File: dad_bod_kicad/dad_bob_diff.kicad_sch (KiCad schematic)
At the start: 66 parts

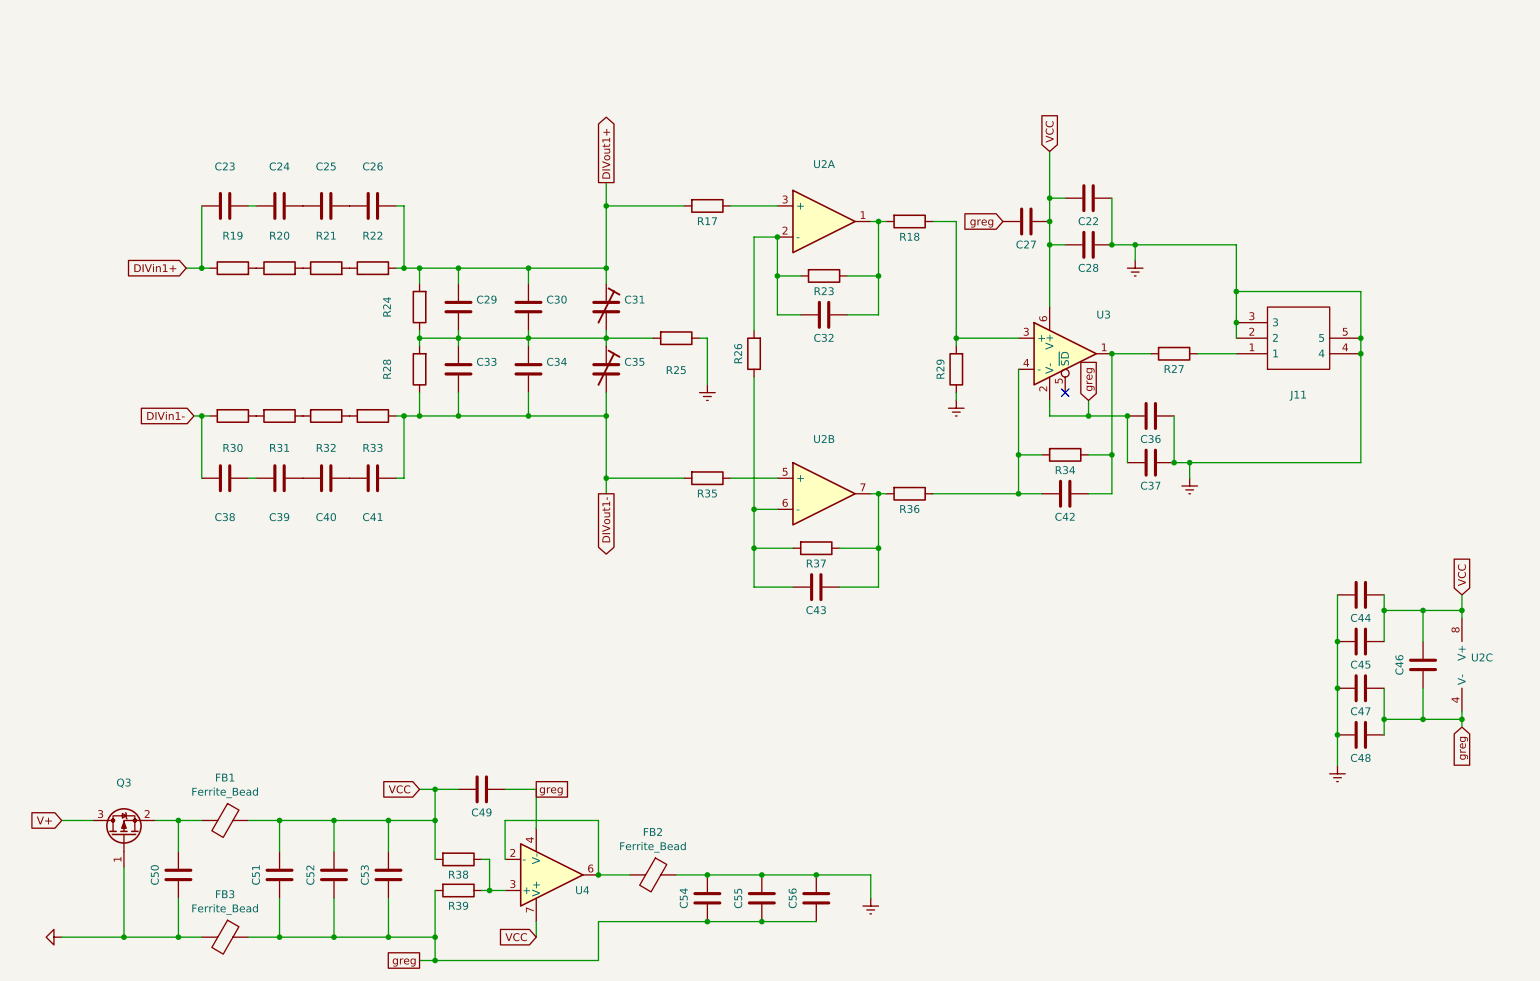
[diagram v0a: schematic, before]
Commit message: Routed board
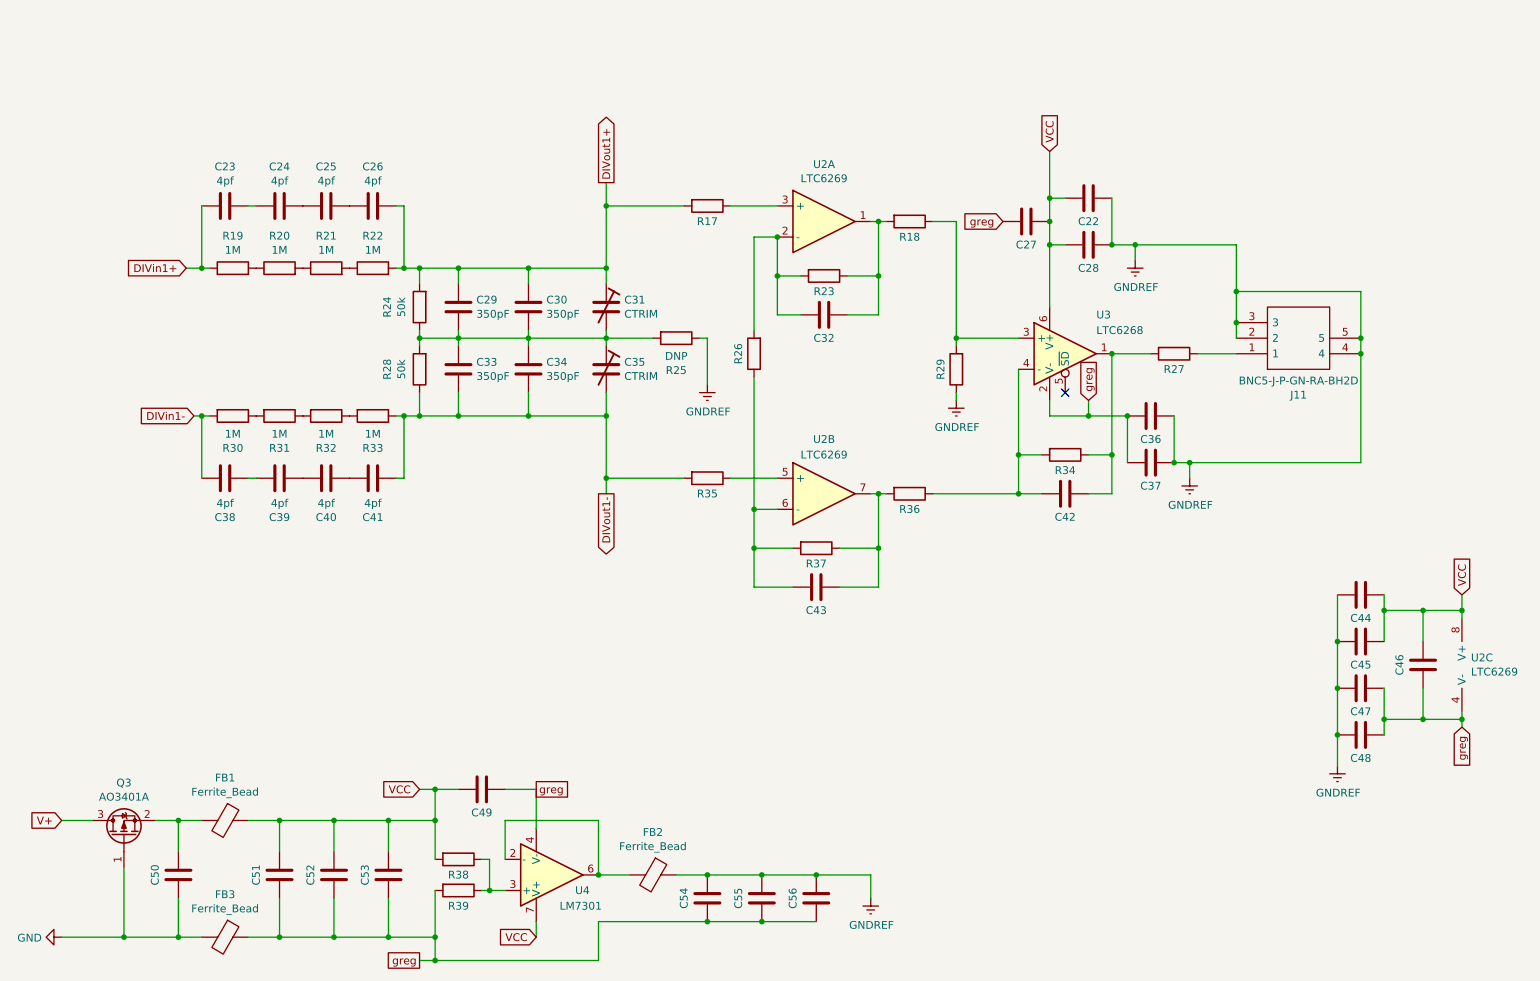
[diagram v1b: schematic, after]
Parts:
- C22, C27, C28, C32, C36, C37, C42, C43, C44, C45, C46, C47, C48, C49, C50, C51, C52, C53, C54, C55, C56: value (none) -> ~; footprint (none) -> Capacitor_SMD:C_0805_2012Metric_Pad1.15x1.40mm_HandSolder
- C23, C24, C25, C26, C38, C39, C40, C41: value (none) -> 4pf; footprint (none) -> Capacitor_SMD:C_0805_2012Metric_Pad1.15x1.40mm_HandSolder
- C29, C30, C33, C34: value (none) -> 350pF; footprint (none) -> Capacitor_SMD:C_0805_2012Metric_Pad1.15x1.40mm_HandSolder
- C31, C35: value (none) -> CTRIM; footprint (none) -> Capacitor_SMD:C_Trimmer_Voltronics_JQ
- J11: value (none) -> BNC5-J-P-GN-RA-BH2D; footprint (none) -> BNC5-J-P-GN-RA-BH2D_kicad:BNC5JPGNRABH2D
- Q3: value (none) -> AO3401A; footprint (none) -> Package_TO_SOT_SMD:SOT-23
- R17, R18, R23, R26, R27, R29, R34, R35, R36, R37, R38, R39: value (none) -> ~; footprint (none) -> Resistor_SMD:R_0805_2012Metric_Pad1.15x1.40mm_HandSolder
- R19, R20, R21, R22, R30, R31, R32, R33: value (none) -> 1M; footprint (none) -> Resistor_SMD:R_0805_2012Metric_Pad1.15x1.40mm_HandSolder
- R24, R28: value (none) -> 50k; footprint (none) -> Resistor_SMD:R_0805_2012Metric_Pad1.15x1.40mm_HandSolder
- R25: value (none) -> DNP; footprint (none) -> Resistor_SMD:R_0805_2012Metric_Pad1.15x1.40mm_HandSolder
- U2: value (none) -> LTC6269; footprint (none) -> LTC6269:SOP65P490X110-9N
- U3: value (none) -> LTC6268; footprint (none) -> LTC6268IS6-10#TRMPBF:SOT95P280X100-6N
- U4: value (none) -> LM7301; footprint (none) -> LTC6269:SOP65P490X110-9N

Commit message: changed some routing/footprints after component selection
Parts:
- added D7, D8: BAV199-TP, kyuditsky_kicad:bav199_tp_SOT95P237X125-3N, symbol BAV199-TP:BAV199-TP
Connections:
- net DIVout1+: now also D8.3 (A/K)
- net DIVout1-: now also D7.3 (A/K)
- net VCC: now also D7.2 (K), D8.2 (K)
- net greg: now also D7.1 (A), D8.1 (A)
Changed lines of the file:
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@@
   (junction (at 121.92 85.09) (diameter 0) (color 0 0 0 0)
   )
+  (junction (at 102.235 97.79) (diameter 0) (color 0 0 0 0)
+  )
   (junction (at 245.11 85.09) (diameter 0) (color 0 0 0 0)
   )
@@
   )
   (junction (at 189.23 110.49) (diameter 0) (color 0 0 0 0)
+  )
+  (junction (at 106.68 73.66) (diameter 0) (color 0 0 0 0)
   )
   (junction (at 93.98 186.69) (diameter 0) (color 0 0 0 0)
@@
     (stroke (width 0) (type default) (color 0 0 0 0))
   )
+  (wire (pts (xy 106.68 46.355) (xy 106.68 40.005))
+    (stroke (width 0) (type default) (color 0 0 0 0))
+  )
   (wire (pts (xy 245.11 77.47) (xy 245.11 85.09))
     (stroke (width 0) (type default) (color 0 0 0 0))
@@
     (stroke (width 0) (type default) (color 0 0 0 0))
   )
-  (wire (pts (xy 97.79 97.79) (xy 109.22 97.79))
+  (wire (pts (xy 97.79 97.79) (xy 102.235 97.79))
     (stroke (width 0) (type default) (color 0 0 0 0))
   )
@@
     (stroke (width 0) (type default) (color 0 0 0 0))
   )
+  (wire (pts (xy 102.235 125.095) (xy 102.235 131.445))
+    (stroke (width 0) (type default) (color 0 0 0 0))
+  )
   (wire (pts (xy 133.35 172.72) (xy 138.43 172.72))
     (stroke (width 0) (type default) (color 0 0 0 0))
@@
     (stroke (width 0) (type default) (color 0 0 0 0))
   )
+  (wire (pts (xy 102.235 97.79) (xy 102.235 102.235))
+    (stroke (width 0) (type default) (color 0 0 0 0))
+  )
   (wire (pts (xy 121.92 76.2) (xy 121.92 73.66))
     (stroke (width 0) (type default) (color 0 0 0 0))
@@
     (stroke (width 0) (type default) (color 0 0 0 0))
   )
+  (wire (pts (xy 102.235 97.79) (xy 109.22 97.79))
+    (stroke (width 0) (type default) (color 0 0 0 0))
+  )
   (wire (pts (xy 120.65 163.83) (xy 120.65 172.72))
     (stroke (width 0) (type default) (color 0 0 0 0))
@@
     (stroke (width 0) (type default) (color 0 0 0 0))
   )
+  (wire (pts (xy 106.68 73.66) (xy 109.22 73.66))
+    (stroke (width 0) (type default) (color 0 0 0 0))
+  )
   (wire (pts (xy 87.63 107.95) (xy 88.9 107.95))
     (stroke (width 0) (type default) (color 0 0 0 0))
@@
     (stroke (width 0) (type default) (color 0 0 0 0))
   )
-  (wire (pts (xy 97.79 73.66) (xy 109.22 73.66))
+  (wire (pts (xy 97.79 73.66) (xy 106.68 73.66))
     (stroke (width 0) (type default) (color 0 0 0 0))
   )
@@
   )
   (wire (pts (xy 93.98 163.83) (xy 93.98 170.18))
+    (stroke (width 0) (type default) (color 0 0 0 0))
+  )
+  (wire (pts (xy 106.68 69.215) (xy 106.68 73.66))
     (stroke (width 0) (type default) (color 0 0 0 0))
   )
@@
     )
   )
+  (global_label "greg" (shape input) (at 106.68 40.005 90) (fields_autoplaced)
+    (effects (font (size 1.27 1.27)) (justify left))
+    (property "Intersheet References" "${INTERSHEET_REFS}" (id 0) (at 172.72 -146.685 0)
+      (effects (font (size 1.27 1.27)) hide)
+    )
+  )
+  (global_label "VCC" (shape input) (at 104.775 125.095 270) (fields_autoplaced)
+    (effects (font (size 1.27 1.27)) (justify right))
+    (property "Intersheet References" "${INTERSHEET_REFS}" (id 0) (at -53.975 216.535 0)
+      (effects (font (size 1.27 1.27)) hide)
+    )
+  )
   (global_label "greg" (shape passive) (at 91.44 186.69 180) (fields_autoplaced)
     (effects (font (size 1.27 1.27)) (justify right))
@@
     )
   )
+  (global_label "VCC" (shape input) (at 104.14 46.355 90) (fields_autoplaced)
+    (effects (font (size 1.27 1.27)) (justify left))
+    (property "Intersheet References" "${INTERSHEET_REFS}" (id 0) (at 262.89 -45.085 0)
+      (effects (font (size 1.27 1.27)) hide)
+    )
+  )
   (global_label "DIVin1+" (shape input) (at 53.34 73.66 180) (fields_autoplaced)
     (effects (font (size 1.27 1.27)) (justify right))
@@
     (effects (font (size 1.27 1.27)) (justify left))
     (property "Intersheet References" "${INTERSHEET_REFS}" (id 0) (at 0 0 0)
+      (effects (font (size 1.27 1.27)) hide)
+    )
+  )
+  (global_label "greg" (shape input) (at 102.235 131.445 270) (fields_autoplaced)
+    (effects (font (size 1.27 1.27)) (justify right))
+    (property "Intersheet References" "${INTERSHEET_REFS}" (id 0) (at 36.195 318.135 0)
       (effects (font (size 1.27 1.27)) hide)
     )
@@
     (pin "1")
   )
+  (symbol (lib_id "BAV199-TP:BAV199-TP") (at 102.235 125.095 90) (unit 1)
+    (in_bom yes) (on_board yes) (fields_autoplaced)
+    (property "Reference" "D7" (id 0) (at 108.585 112.3949 90)
+      (effects (font (size 1.27 1.27)) (justify right))
+    )
+    (property "Value" "BAV199-TP" (id 1) (at 108.585 114.9349 90)
+      (effects (font (size 1.27 1.27)) (justify right))
+    )
+    (property "Footprint" "kyuditsky_kicad:bav199_tp_SOT95P237X125-3N" (id 2) (at 99.695 106.045 0)
+      (effects (font (size 1.27 1.27)) (justify left) hide)
+    )
+    (property "Datasheet" "https://www.mouser.com/datasheet/2/258/BAV199(SOT-23)-V1-1625900.pdf" (id 3) (at 102.235 106.045 0)
+      (effects (font (size 1.27 1.27)) (justify left) hide)
+    )
+    (property "Description" "Diodes - General Purpose, Power, Switching Dual 215mA, 70V" (id 4) (at 104.775 106.045 0)
+      (effects (font (size 1.27 1.27)) (justify left) hide)
+    )
+    (property "Height" "1.25" (id 5) (at 107.315 106.045 0)
+      (effects (font (size 1.27 1.27)) (justify left) hide)
+    )
+    (property "Manufacturer_Name" "Micro Commercial Components (MCC)" (id 6) (at 109.855 106.045 0)
+      (effects (font (size 1.27 1.27)) (justify left) hide)
+    )
+    (property "Manufacturer_Part_Number" "BAV199-TP" (id 7) (at 112.395 106.045 0)
+      (effects (font (size 1.27 1.27)) (justify left) hide)
+    )
+    (property "Mouser Part Number" "833-BAV199-TP" (id 8) (at 114.935 106.045 0)
+      (effects (font (size 1.27 1.27)) (justify left) hide)
+    )
+    (property "Mouser Price/Stock" "https://www.mouser.co.uk/ProductDetail/Micro-Commercial-Components-MCC/BAV199-TP?qs=O1HRStiETCgJXUOrgD0Lnw%3D%3D" (id 9) (at 117.475 106.045 0)
+      (effects (font (size 1.27 1.27)) (justify left) hide)
+    )
+    (property "Arrow Part Number" "BAV199-TP" (id 10) (at 120.015 106.045 0)
+      (effects (font (size 1.27 1.27)) (justify left) hide)
+    )
+    (property "Arrow Price/Stock" "https://www.arrow.com/en/products/bav199-tp/micro-commercial-components?region=nac" (id 11) (at 122.555 106.045 0)
+      (effects (font (size 1.27 1.27)) (justify left) hide)
+    )
+    (pin "1")
+    (pin "2")
+    (pin "3")
+  )
+  (symbol (lib_id "BAV199-TP:BAV199-TP") (at 106.68 46.355 270) (unit 1)
+    (in_bom yes) (on_board yes) (fields_autoplaced)
+    (property "Reference" "D8" (id 0) (at 100.33 59.0551 90)
+      (effects (font (size 1.27 1.27)) (justify right))
+    )
+    (property "Value" "BAV199-TP" (id 1) (at 100.33 56.5151 90)
+      (effects (font (size 1.27 1.27)) (justify right))
+    )
+    (property "Footprint" "kyuditsky_kicad:bav199_tp_SOT95P237X125-3N" (id 2) (at 109.22 65.405 0)
+      (effects (font (size 1.27 1.27)) (justify left) hide)
+    )
+    (property "Datasheet" "https://www.mouser.com/datasheet/2/258/BAV199(SOT-23)-V1-1625900.pdf" (id 3) (at 106.68 65.405 0)
+      (effects (font (size 1.27 1.27)) (justify left) hide)
+    )
+    (property "Description" "Diodes - General Purpose, Power, Switching Dual 215mA, 70V" (id 4) (at 104.14 65.405 0)
+      (effects (font (size 1.27 1.27)) (justify left) hide)
+    )
+    (property "Height" "1.25" (id 5) (at 101.6 65.405 0)
+      (effects (font (size 1.27 1.27)) (justify left) hide)
+    )
+    (property "Manufacturer_Name" "Micro Commercial Components (MCC)" (id 6) (at 99.06 65.405 0)
+      (effects (font (size 1.27 1.27)) (justify left) hide)
+    )
+    (property "Manufacturer_Part_Number" "BAV199-TP" (id 7) (at 96.52 65.405 0)
+      (effects (font (size 1.27 1.27)) (justify left) hide)
+    )
+    (property "Mouser Part Number" "833-BAV199-TP" (id 8) (at 93.98 65.405 0)
+      (effects (font (size 1.27 1.27)) (justify left) hide)
+    )
+    (property "Mouser Price/Stock" "https://www.mouser.co.uk/ProductDetail/Micro-Commercial-Components-MCC/BAV199-TP?qs=O1HRStiETCgJXUOrgD0Lnw%3D%3D" (id 9) (at 91.44 65.405 0)
+      (effects (font (size 1.27 1.27)) (justify left) hide)
+    )
+    (property "Arrow Part Number" "BAV199-TP" (id 10) (at 88.9 65.405 0)
+      (effects (font (size 1.27 1.27)) (justify left) hide)
+    )
+    (property "Arrow Price/Stock" "https://www.arrow.com/en/products/bav199-tp/micro-commercial-components?region=nac" (id 11) (at 86.36 65.405 0)
+      (effects (font (size 1.27 1.27)) (justify left) hide)
+    )
+    (pin "1")
+    (pin "2")
+    (pin "3")
+  )
 )

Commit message: Added BOMs & db_standalone order
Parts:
- C22, C36, C44, C48, C49, C56: value ~ -> 100n
- C27, C46: value ~ -> 4.7u
- C28, C37, C45, C47: value ~ -> 100p
- C32: value ~ -> 0.2p +/- 0.05p
- C42: value ~ -> 0.4p +/- 0.05p
- C43: value ~ -> 0.2p
- C50, C51, C54: value ~ -> 10u; symbol Device:C -> Device:C_Polarized
- C52: value ~ -> dnp
- C53, C55: value ~ -> 1u
- R17, R35: value ~ -> 1.5k
- R18, R36: value ~ -> 1.02k 0.1%
- R23, R37: value ~ -> 3.92k
- R26: value ~ -> 412
- R27: value ~ -> 51 1%
- R29, R34: value ~ -> 1.27k 0.1%
- R38, R39: value ~ -> 10k
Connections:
- net GND: now also C50.2; no longer C50.1
- net GNDREF: now also C54.1; no longer C54.2
- net VCC: now also C51.1; no longer C51.2
- net greg: now also C51.2, C54.2; no longer C51.1, C54.1
- net at FB1.2, Q3.2 (S): now also C50.1; no longer C50.2
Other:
- note added: "find replacement M1"
